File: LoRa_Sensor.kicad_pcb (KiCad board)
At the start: 2 copper layers, 40 x 86 mm, 28 parts, among them IC1 BME688, J1 Conn_01x02_Pin, J2 TC2030-IDC-NL, U1 RAK3172_MODULE, U2 2462

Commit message: done for the day :)
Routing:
- net GND: vias 26 -> 32
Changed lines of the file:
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@@
   (gr_arc (start 126 42) (mid 128.828427 43.171573) (end 130 46)
     (stroke (width 0.1) (type default)) (layer "Edge.Cuts"))
+  (gr_text "JLCJLCJLCJLC" (at 110 52.75) (layer "B.SilkS")
+    (effects (font (size 1 1) (thickness 0.15)) (justify bottom mirror))
+  )
+  (gr_text "AV PROTO\nLow Power\nLoRa Environmental Sensor\n* EU868 *\nV0.2 - Batch 1" (at 110 47.25) (layer "B.SilkS")
+    (effects (font (size 1 1) (thickness 0.15)) (justify mirror))
+  )
   (gr_text "+" (at 125.7 67.475) (layer "F.SilkS")
     (effects (font (size 2 2) (thickness 0.25)))
-  )
-  (gr_text "JLCJLCJLCJLC" (at 69 104.25) (layer "F.SilkS")
-    (effects (font (size 1 1) (thickness 0.15)) (justify bottom))
-  )
-  (gr_text "AV PROTO\nLow Power\nLoRa Environmental Sensor\n* EU868 *\nV0.2 - Batch 1" (at 70 97.25) (layer "F.SilkS")
-    (effects (font (size 1 1) (thickness 0.15)))
   )
   (gr_text "-" (at 125.7 64.975) (layer "F.SilkS")
@@
   (via (at 114 57) (size 0.8) (drill 0.4) (layers "F.Cu" "B.Cu") (free) (net 1))
   (via (at 114 55) (size 0.8) (drill 0.4) (layers "F.Cu" "B.Cu") (free) (net 1))
+  (via (at 113 57) (size 0.8) (drill 0.4) (layers "F.Cu" "B.Cu") (free) (net 1))
+  (via (at 113 56) (size 0.8) (drill 0.4) (layers "F.Cu" "B.Cu") (free) (net 1))
   (via (at 122.2125 107) (size 0.8) (drill 0.4) (layers "F.Cu" "B.Cu") (net 1))
+  (via (at 113 55) (size 0.8) (drill 0.4) (layers "F.Cu" "B.Cu") (free) (net 1))
   (via (at 116.25 70.5) (size 0.8) (drill 0.4) (layers "F.Cu" "B.Cu") (net 1))
   (via (at 106.25 56.75) (size 0.8) (drill 0.4) (layers "F.Cu" "B.Cu") (net 1))
@@
   (via (at 123.25 55.25) (size 0.8) (drill 0.4) (layers "F.Cu" "B.Cu") (net 1))
   (via (at 116 56) (size 0.8) (drill 0.4) (layers "F.Cu" "B.Cu") (free) (net 1))
+  (via (at 117 56) (size 0.8) (drill 0.4) (layers "F.Cu" "B.Cu") (free) (net 1))
   (via (at 114 56) (size 0.8) (drill 0.4) (layers "F.Cu" "B.Cu") (free) (net 1))
   (via (at 113 107.5) (size 0.8) (drill 0.4) (layers "F.Cu" "B.Cu") (net 1))
+  (via (at 117 57) (size 0.8) (drill 0.4) (layers "F.Cu" "B.Cu") (free) (net 1))
   (via (at 115 55) (size 0.8) (drill 0.4) (layers "F.Cu" "B.Cu") (net 1))
   (via (at 115 56) (size 0.8) (drill 0.4) (layers "F.Cu" "B.Cu") (free) (net 1))
@@
   (via (at 116 55) (size 0.8) (drill 0.4) (layers "F.Cu" "B.Cu") (free) (net 1))
   (via (at 122.25 97) (size 0.8) (drill 0.4) (layers "F.Cu" "B.Cu") (net 1))
+  (via (at 117 55) (size 0.8) (drill 0.4) (layers "F.Cu" "B.Cu") (free) (net 1))
   (via (at 122.25 102) (size 0.8) (drill 0.4) (layers "F.Cu" "B.Cu") (net 1))
   (segment (start 128.75 60.75) (end 128.75 56.25) (width 0.25) (layer "F.Cu") (net 2))
@@
     (polygon
       (pts
-        (xy 113.5 54.5)
-        (xy 116.5 54.5)
-        (xy 116.5 57.5)
-        (xy 113.5 57.5)
+        (xy 112.5 54.5)
+        (xy 117.5 54.5)
+        (xy 117.5 57.5)
+        (xy 112.5 57.5)
       )
     )

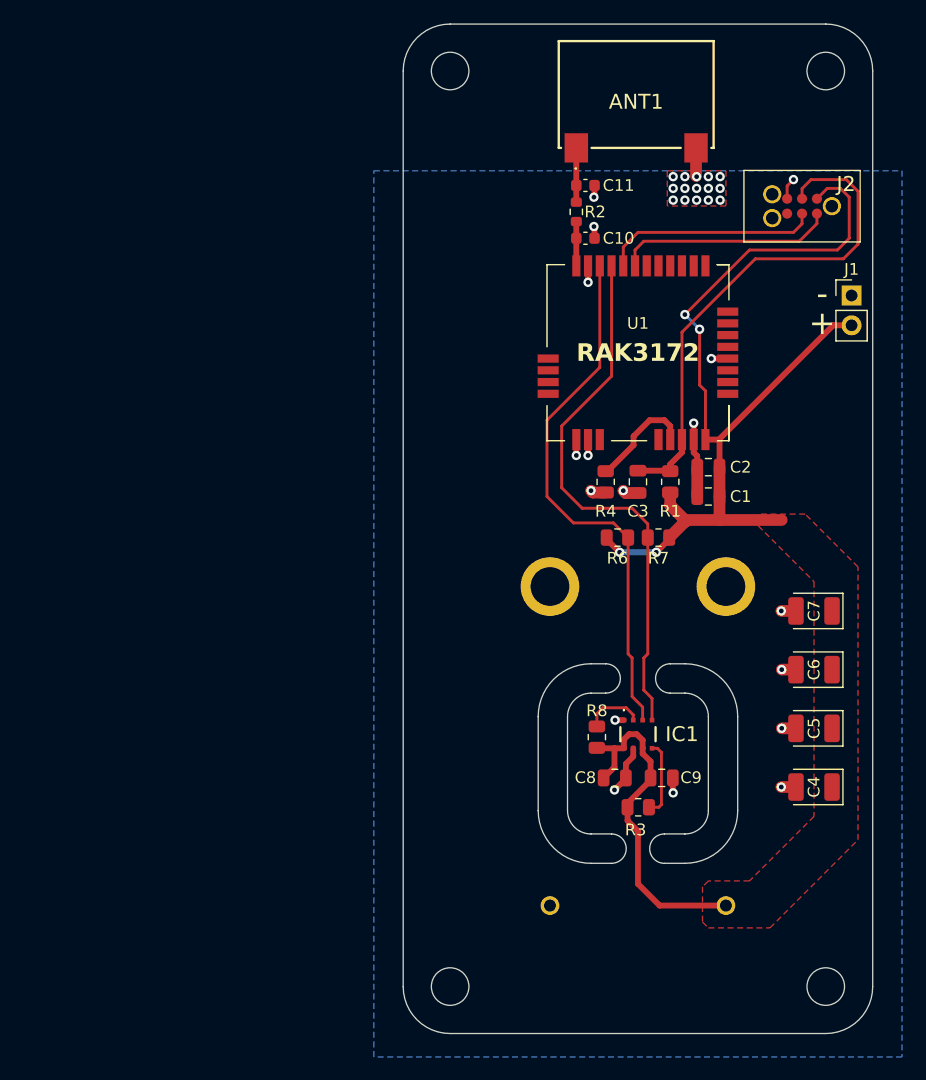
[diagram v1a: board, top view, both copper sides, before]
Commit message: add checkboxes for frequency
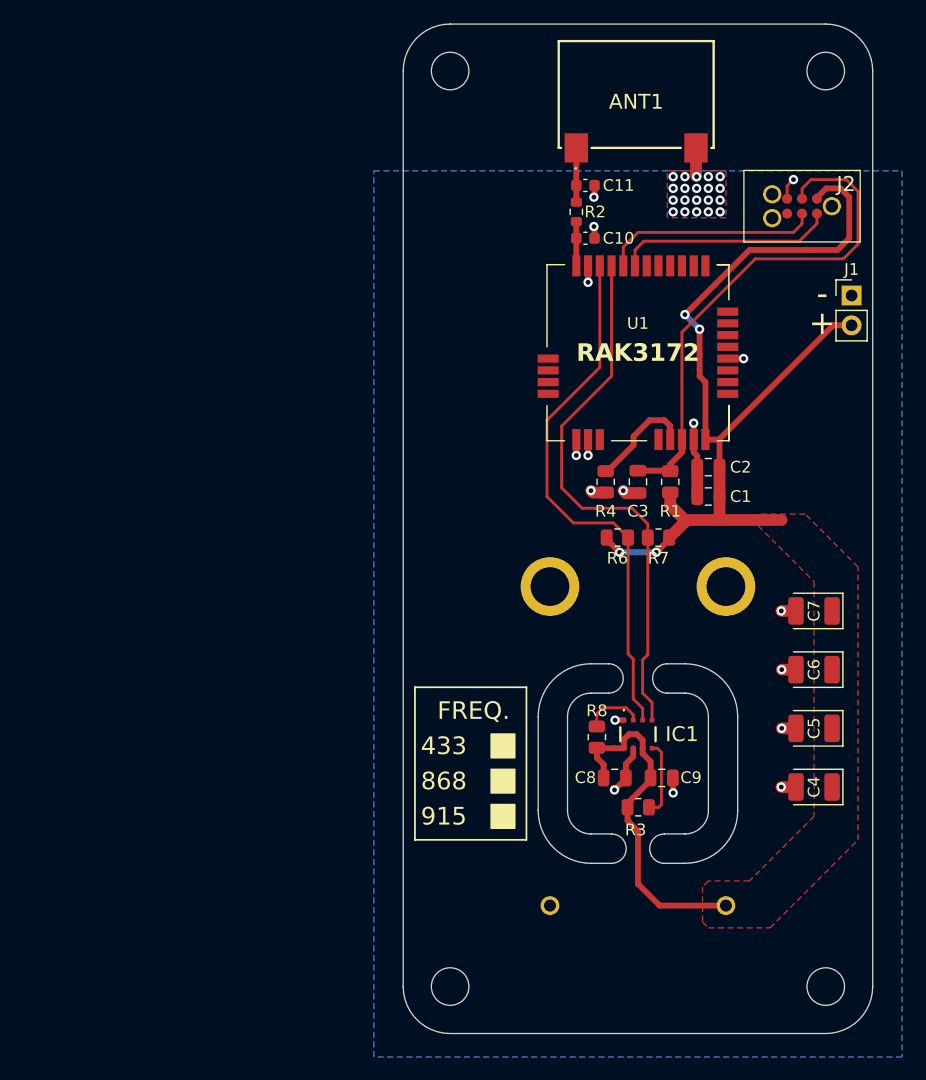
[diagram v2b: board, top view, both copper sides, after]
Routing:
- net GND: track 32.0 -> 31.9 mm, vias 32 -> 37
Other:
- outline, holes or cut-outs redrawn
- board text added: "433"
- board text added: "868"
- board text added: "915"
- board text added: "AV PROTO Low Power LoRa Environmental Sensor V0.2 - Batch 1"
- board text added: "FREQ."
- board text removed: "AV PROTO Low Power LoRa Environmental Sensor * EU868 * V0.2 - Batch 1"
